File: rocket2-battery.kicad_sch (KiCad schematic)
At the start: 82 parts, among them J2 Conn_01x07, J3 USB-C, J4 SMA, J5 ARM Cortex Debug, Q2 Q_NMOS_GSD, Q3 Q_NMOS_GSD, Q4 PMOS, Q5 PMOS, Q6 Q_NMOS_GSD, Q7 Q_NMOS_GSD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

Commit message: ALMOST
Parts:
- removed R13, R18: 15K, Resistor_SMD:R_0402_1005Metric, symbol Device:R_Small_US
- removed R16, R9: 100K, Resistor_SMD:R_0402_1005Metric, symbol Device:R_Small_US
- added C7: 100nF, Capacitor_SMD:C_0402_1005Metric, symbol Device:C_Small
- added R117, R7: 15K, Resistor_SMD:R_0402_1005Metric, symbol Device:R_Small_US
- added R6, R8: 100K, Resistor_SMD:R_0402_1005Metric, symbol Device:R_Small_US
- added U44, U5: ~, Package_TO_SOT_SMD:SOT-23-5, symbol UCIRP-KiCAD-Lib:MCP6001
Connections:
- net +3V3_REDS: now also C7.1, U44.5 (V+), U5.5 (V+)
- net BATT_IN+: now also R8.1
- net GND: now also C7.2, R117.2, R7.2, U44.2 (V-), U5.2 (V-)
- net GSE_IN+: now also R6.1
- net REDs_V_SENSE1: now also U5.1, U5.4 (-)
- net REDs_V_SENSE2: now also U44.1, U44.4 (-)
- net Single-Cell-Charger1/BAT-: now also J2.3 (Pin_3)
- net Single-Cell-Charger3/BAT-: now also J2.5 (Pin_5)
- net REDs_SCL: no longer names the net of U8.42 (PB6)
- net REDs_SDA: no longer names the net of U8.43 (PB7)
- new net: R117.1, R8.2, U44.3 (+)
- new net: R6.2, R7.1, U5.3 (+)
- no-connect marks 42 -> 44
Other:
- note added: "V_Sense REDS"
- note removed: "V_Sense"
- moved on the sheet: C101, C102, C103, C104, C105, D2, D4, D40, L3, R125, TP21, U50

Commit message: layout done
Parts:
- J4: footprint Connector_Coaxial:SMA_Molex_73251-2200_Horizontal -> 0UCIRP-KiCAD-Lib:CONN_73391-0070_MOL
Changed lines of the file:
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@@
 			)
 		)
-		(property "Footprint" "Connector_Coaxial:SMA_Molex_73251-2200_Horizontal"
+		(property "Footprint" "0UCIRP-KiCAD-Lib:CONN_73391-0070_MOL"
 			(at 297.18 93.98 0)
 			(effects
@@
 			)
 		)
-		(property "Datasheet" "https://www.molex.com/en-us/products/part-detail/732512200?display=pdf"
+		(property "Datasheet" "https://www.molex.com/en-us/products/part-detail/733910070?display=pdf"
 			(at 297.18 93.98 0)
 			(effects

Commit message: version in PCBway 12/12/2025
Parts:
- D2, D4: Part # (none) -> V3FM15-M3/H
- J2: now not fitted
- U9: Part # RFM96W -> RFM95W; now not fitted
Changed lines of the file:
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@@
 		(in_bom yes)
 		(on_board yes)
-		(dnp no)
+		(dnp yes)
 		(fields_autoplaced yes)
 		(property "Reference" "J2"
@@
 		(in_bom yes)
 		(on_board yes)
-		(dnp no)
+		(dnp yes)
 		(property "Reference" "U9"
 			(at 325.12 57.15 0)
@@
 			)
 		)
-		(property "Part #" "RFM96W"
+		(property "Part #" "RFM95W"
 			(at 325.12 62.23 0)
 			(effects
@@
 			)
 		)
+		(property "Part #" "V3FM15-M3/H "
+			(at 157.48 199.39 0)
+			(effects
+				(font
+					(size 1.27 1.27)
+				)
+				(hide yes)
+			)
+		)
 		(pin "1"
 		)
@@
 			(at 157.48 191.77 0)
 			(effects
+				(font
+					(size 1.27 1.27)
+				)
+				(hide yes)
+			)
+		)
+		(property "Part #" "V3FM15-M3/H "
+			(at 157.48 191.77 0)
+			(effects

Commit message: added some production files
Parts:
- D1, D7: Part # SDT8A100P5-7 -> SBR10E45P5-13
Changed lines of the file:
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@@
 			)
 		)
-		(property "Datasheet" "https://www.diodes.com/assets/Datasheets/SDT8A100P5.pdf"
+		(property "Datasheet" "https://www.diodes.com/assets/Datasheets/SBR10E45P5.pdf"
 			(at 295.91 123.19 90)
 			(effects
@@
 			)
 		)
-		(property "Part #" "SDT8A100P5-7"
+		(property "Part #" "SBR10E45P5-13"
 			(at 295.91 123.19 0)
 			(effects
@@
 			)
 		)
-		(property "Datasheet" "https://www.diodes.com/assets/Datasheets/SDT8A100P5.pdf"
+		(property "Datasheet" "https://www.diodes.com/assets/Datasheets/SBR10E45P5.pdf"
 			(at 200.66 123.19 90)
 			(effects
@@
 			)
 		)
-		(property "Part #" "SDT8A100P5-7"
+		(property "Part #" "SBR10E45P5-13"
 			(at 200.66 123.19 0)
 			(effects

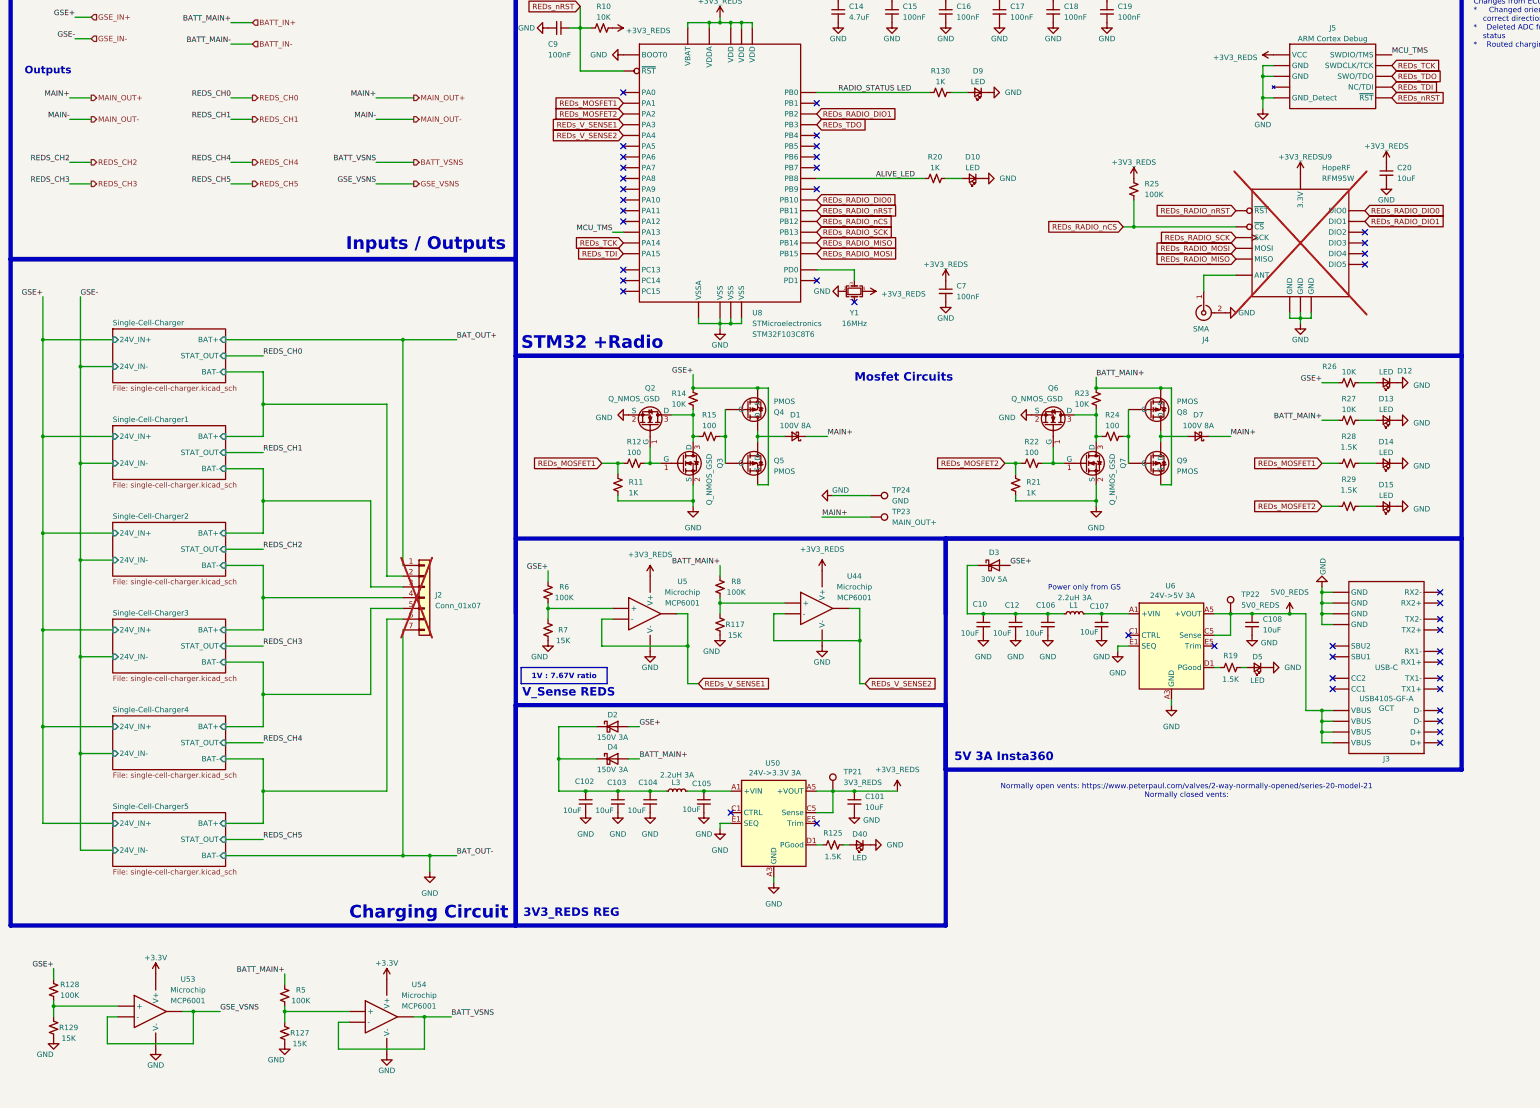
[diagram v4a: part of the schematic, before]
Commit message: changed charging circuit for Insta360, gonna send in now on JLCPCB
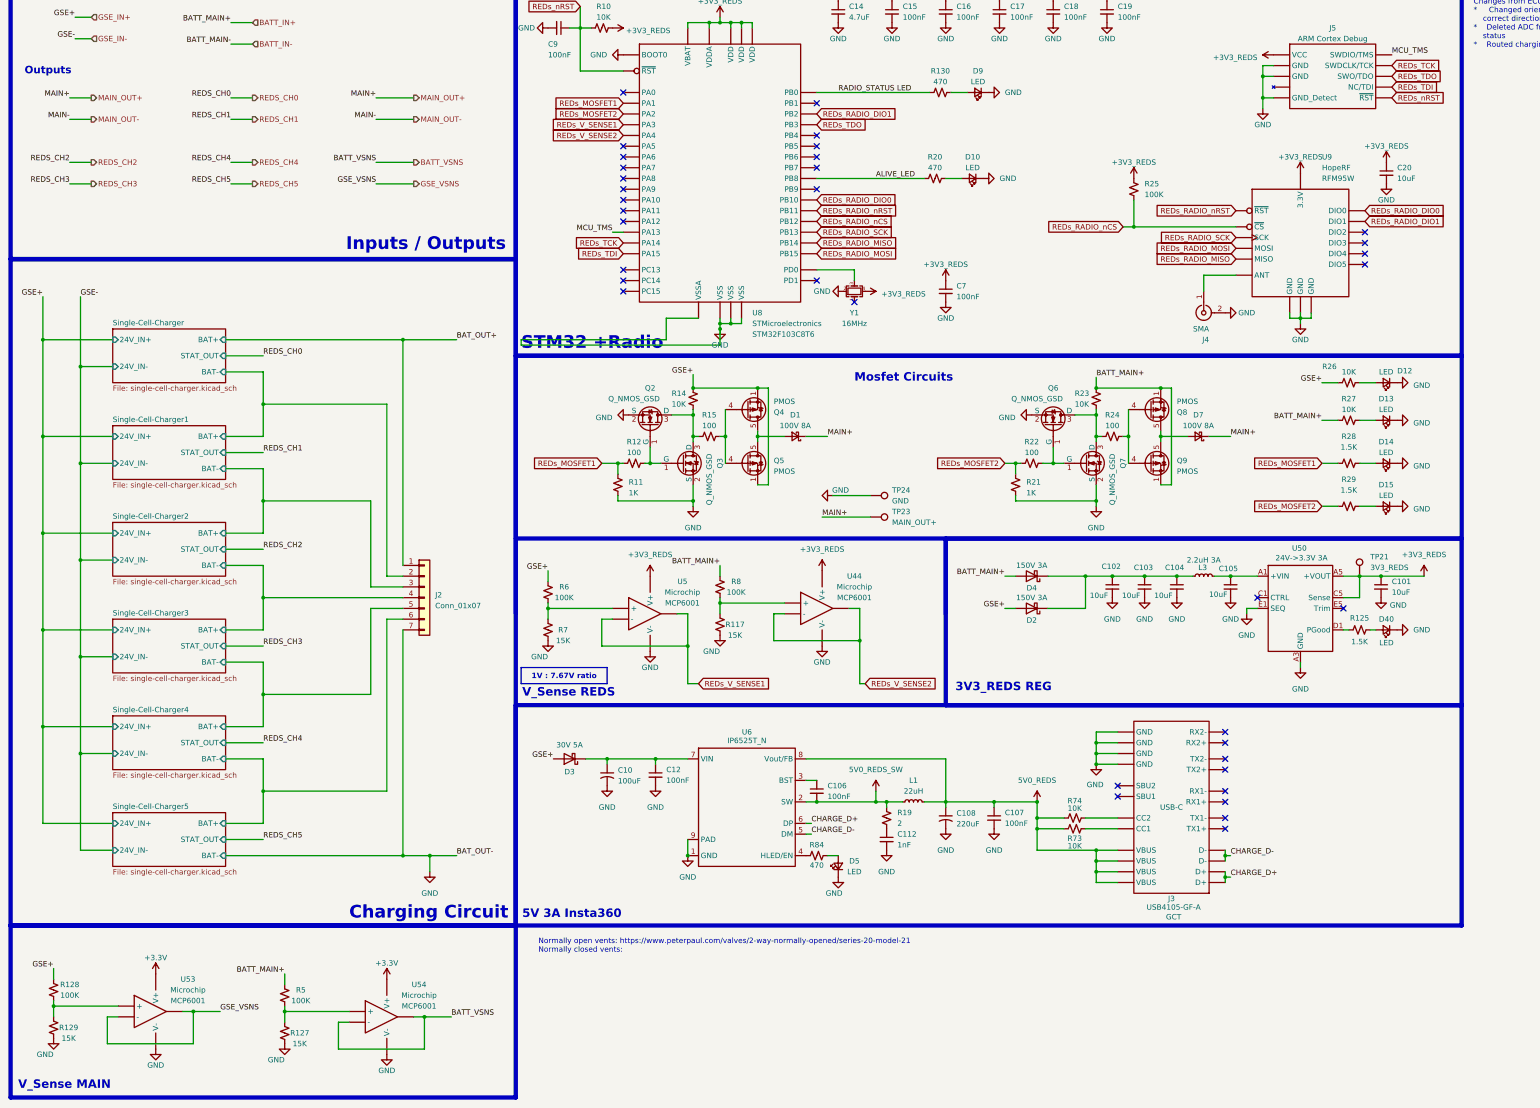
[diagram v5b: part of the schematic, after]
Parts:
- removed C10: 10uF, Capacitor_SMD:C_1210_3225Metric, symbol Device:C_Small
- removed C108: 10uF, Capacitor_SMD:C_1206_3216Metric, symbol Device:C_Small
- removed TP22: 5V0_REDS, TestPoint:TestPoint_Plated_Hole_D2.0mm, symbol Connector:TestPoint
- removed U6: 24V->5V 3A, Converter_DCDC:Converter_DCDC_RECOM_RPMx.x-x.0, symbol Converter_DCDC:RPM3.3-6.0
- added C10: 100uF, Capacitor_SMD:CP_Elec_8x6.7, symbol Device:C_Small_US
- added C108: 220uF, 0UCIRP-KiCAD-Lib:CAP_A768KS227M1VLAE024_KEM, symbol Device:C_Small_US
- added C112: 1nF, Capacitor_SMD:C_0603_1608Metric, symbol Device:C_Small
- added R73, R74: 10K, Resistor_SMD:R_0402_1005Metric, symbol Device:R_Small_US
- added R84: 470, Resistor_SMD:R_0402_1005Metric, symbol Device:R_Small_US
- added U6: ~, 0UCIRP-KiCAD-Lib:IP6525T_N, symbol 0UCIRP-KiCAD-Lib:IP6525T_N
- C106, C107, C12: value 10uF -> 100nF; footprint Capacitor_SMD:C_1210_3225Metric -> Capacitor_SMD:C_0603_1608Metric; Manufacturer Generic -> (none); Part # Generic CAP CER 10UF 50V X7R 1210 -> (none)
- D5: Part # Generic 0603 Yellow-Green LED -> Generic 0603 Red LED
- J2, U9: now fitted
- L1: value 2.2uH 3A -> 22uH; footprint Inductor_SMD:L_Vishay_IHLP-1212 -> Inductor_SMD:L_Sunlord_MWSA1205S-220; Manufacturer Vishay Dale -> (none); Part # IHLP1212BZER2R2M11 -> (none)
- L3: Part # IHLP1212BZER2R2M11 -> IHLP1212BZEV2R2MA1
- R130, R20: value 1K -> 470
- R19: value 1.5K -> 2; footprint Resistor_SMD:R_0402_1005Metric -> Resistor_SMD:R_0603_1608Metric; Part # Generic RES SMD 1.5K OHM 0.1% 1/16W 0402 -> Generic RES SMD 100 OHM 1% 1/4W 0402
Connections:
- net 5V0_REDS: now also C107.1, L1.2, C108.1, R73.2, R74.2, U6.8 (Vout/FB)
- net GND: now also C10.2, C108.2, C112.2, U6.1 (GND), U6.9 (PAD); no longer C106.2
- net at R19.1: now also C112.1
- net at C12.1, D3.1 (K): now also C10.1, U6.7 (VIN); no longer C106.1, L1.1
- net at D5.2 (A): now also R84.2; no longer R19.2
- net at J3.A5 (CC1): now also R73.1
- net CHARGE_D+: now reaches J3.A6 (D+)
- net CHARGE_D+: now also J3.B6 (D+), U6.6 (DP)
- net CHARGE_D-: now reaches J3.A7 (D-)
- net CHARGE_D-: now also J3.B7 (D-), U6.5 (DM)
- net at J3.B5 (CC2): now also R74.1
- new net: R84.1, U6.4 (HLED/EN)
- new net: C106.1, U6.3 (BST)
- new net 5V0_REDS_SW: C106.2, L1.1, R19.2, U6.2 (SW)
- no-connect marks 44 -> 36
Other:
- note added: "V_Sense MAIN"
- note removed: "Power only from GS"
- moved on the sheet: C101, C102, C103, C104, C105, D2, D3, D4, D40, J3, L3, R125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
